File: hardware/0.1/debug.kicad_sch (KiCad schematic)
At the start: 9 parts

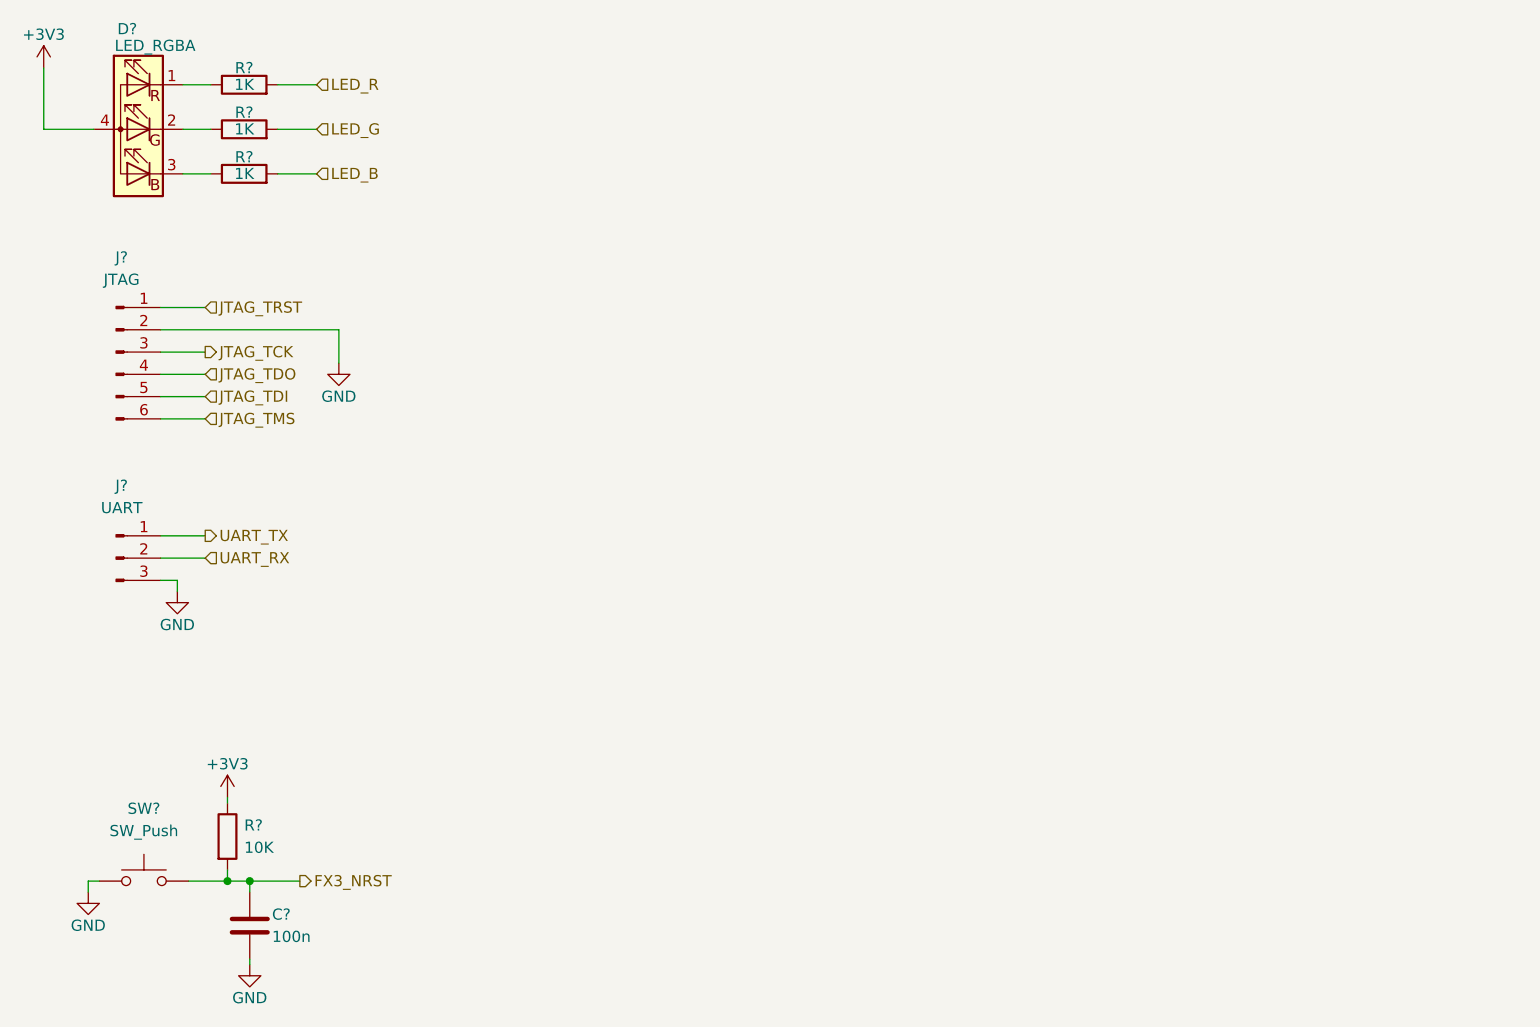
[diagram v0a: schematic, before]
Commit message: first pass schematic done
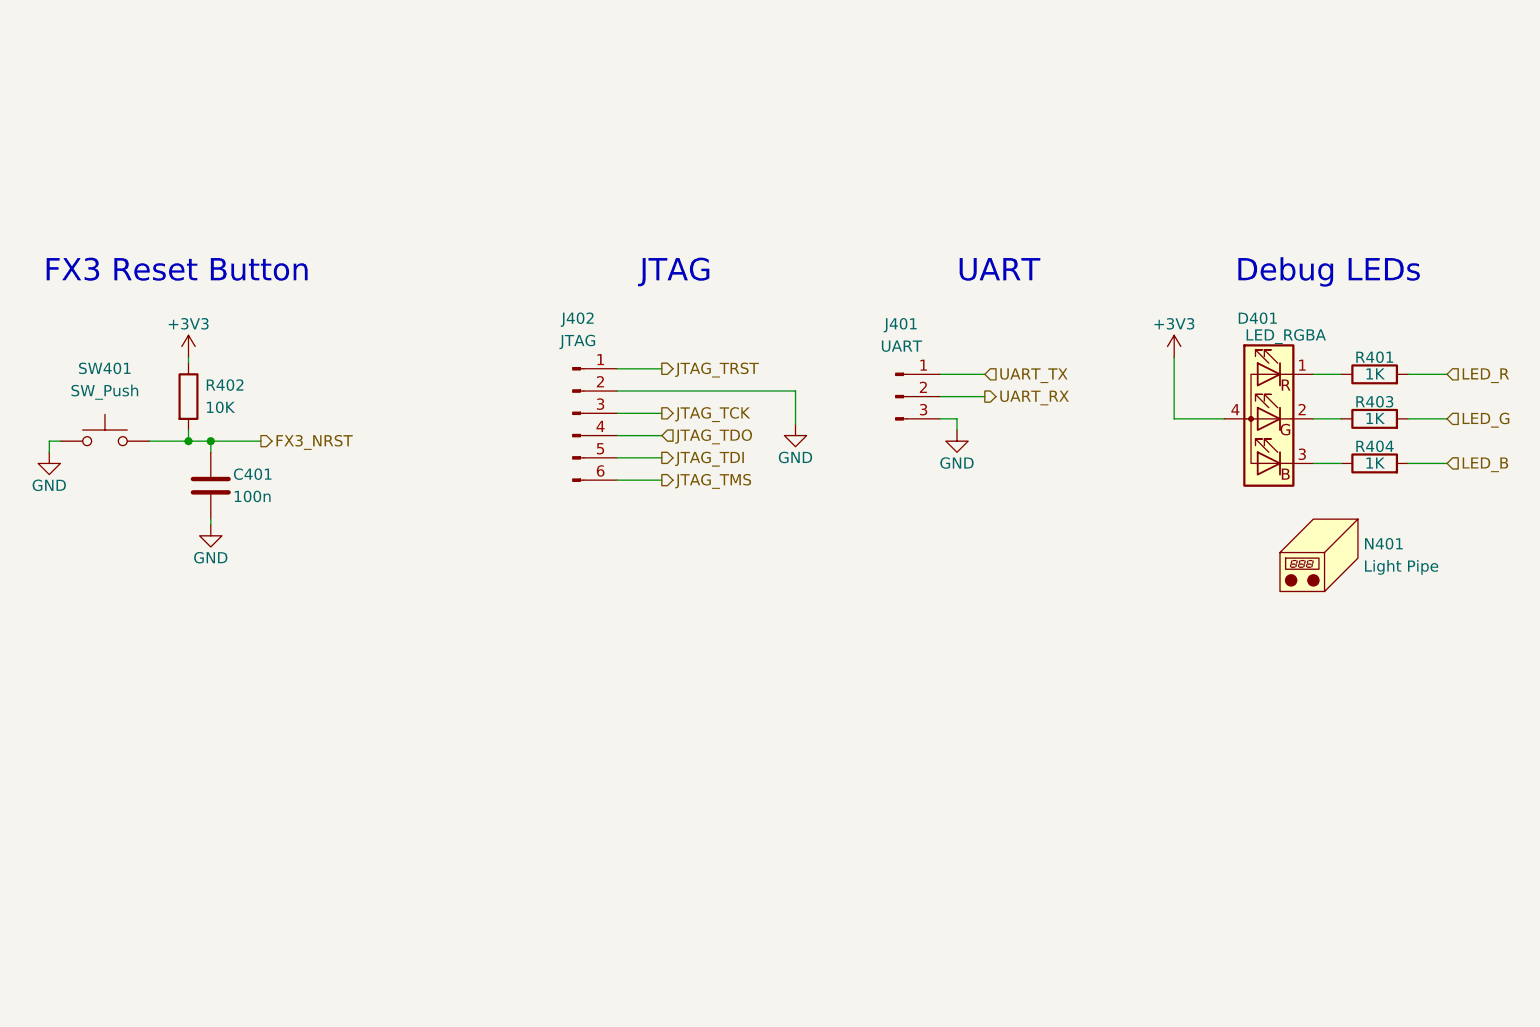
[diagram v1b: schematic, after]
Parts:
- added N401: Light Pipe, symbol Mechanical:Housing
- C401: renamed from C?; footprint (none) -> Capacitor_SMD:C_0402_1005Metric; LCSC (none) -> C307331; MPN (none) -> CL05B104KB54PNC; Manufacturer (none) -> Samsung Electro-Mechanics
- D401: renamed from D?; footprint (none) -> josh-led:LED_TRI_2020; LCSC (none) -> C108793; MPN (none) -> FM-B2020RGBA-HG; Manufacturer (none) -> Foshan NationStar Optoelectronics
- J401, J402: renamed from J?; now left out of the parts list
- R401, R403, R404: renamed from R?; footprint (none) -> Resistor_SMD:R_0402_1005Metric; LCSC (none) -> C144789; MPN (none) -> AC0402FR-071KL; Manufacturer (none) -> Yageo
- R402: renamed from R?; footprint (none) -> Resistor_SMD:R_0402_1005Metric; LCSC (none) -> C60490; MPN (none) -> RC0402FR-0710KL; Manufacturer (none) -> Yageo
- SW401: renamed from SW?; footprint (none) -> josh-buttons-switches:SW_PUSH_EVQPUL_EVQPUC; LCSC (none) -> C79174; MPN (none) -> EVQPUC02K; Manufacturer (none) -> Panasonic
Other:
- note added: "Debug LEDs"
- note added: "FX3 Reset Button"
- note added: "JTAG"
- note added: "UART"
- company: (none) -> Josh Johnson
- title: (none) -> Voyager Logic
- moved on the sheet: C401, D401, J401, J402, R401, R402, R403, R404, SW401

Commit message: finalise BOM
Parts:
- removed J401: UART, symbol Connector:Conn_01x03_Male
- removed N401: Light Pipe, symbol Mechanical:Housing
- added D402: LED_RGBA, josh-led:LED_TRI_2020, symbol josh-led:LED_RGBA
- added J401: JTAG, Connector:Tag-Connect_TC2030-IDC-NL_2x03_P1.27mm_Vertical, symbol Connector:Conn_01x06_Male
- added R405, R406, R407: 1K, Resistor_SMD:R_0402_1005Metric, symbol Device:R
- added R408: DNP, Resistor_SMD:R_0402_1005Metric, symbol Device:R
- added R409: 0R0, Resistor_SMD:R_0402_1005Metric, symbol Device:R
- J402: footprint (none) -> Connector:Tag-Connect_TC2030-IDC-NL_2x03_P1.27mm_Vertical
- SW401: value SW_Push -> KMR2; footprint josh-buttons-switches:SW_PUSH_EVQPUL_EVQPUC -> josh-buttons-switches:SW_Push_KMR2; LCSC C79174 -> (none); MPN EVQPUC02K -> (none); Manufacturer Panasonic -> (none)
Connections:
- net +3V3: now also D402.4 (A), R408.2
- net GND: now also J402.5 (Pin_5), J401.3 (Pin_3), R405.2, R406.2, R407.2; no longer J402.2 (Pin_2)
- net JTAG_TCK: now also J402.4 (Pin_4); no longer J402.3 (Pin_3)
- net JTAG_TDI: now also J402.3 (Pin_3); no longer J402.5 (Pin_5)
- net JTAG_TDO: now also J402.6 (Pin_6); no longer J402.4 (Pin_4)
- net JTAG_TMS: now also J402.2 (Pin_2); no longer J402.6 (Pin_6)
- net JTAG_TRST: now also R409.2; no longer J402.1 (Pin_1)
- net UART_RX: now also J401.2 (Pin_2)
- net UART_TX: now also J401.1 (Pin_1)
- new net: D402.1 (RK), R405.1
- new net: D402.2 (GK), R406.1
- new net: D402.3 (BK), R407.1
- new net: J402.1 (Pin_1), R408.1, R409.1
- no-connect marks 0 -> 3
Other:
- note added: "Digilent HS2/3 pinout has 3v3 on pin 1 We need to breakout JTAG_TRST So placing them on the same pin"
- note added: "Used for power indication"

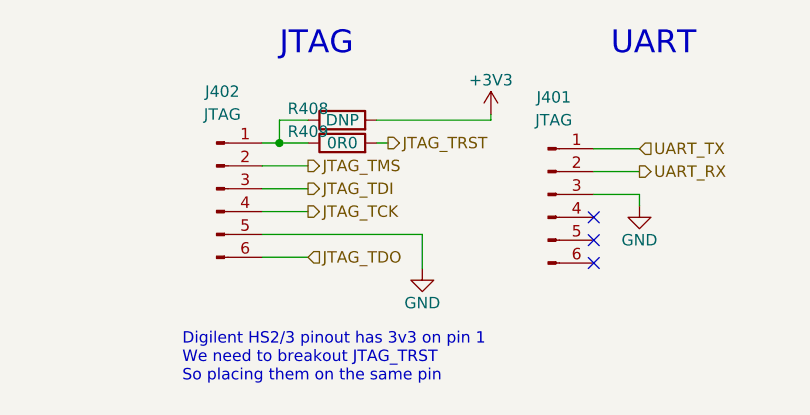
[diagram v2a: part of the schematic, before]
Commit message: all components fit inside outline
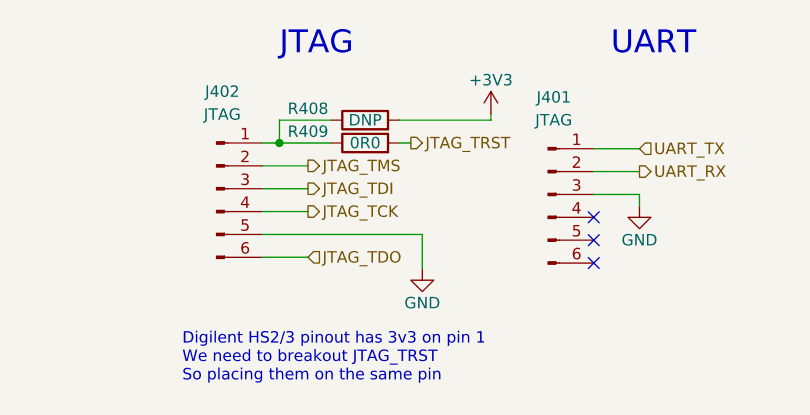
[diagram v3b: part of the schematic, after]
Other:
- moved on the sheet: R408, R409
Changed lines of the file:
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@@
+    (stroke (width 0) (type default) (color 0 0 0 0))
+  )
+  (wire (pts (xy 128.27 97.79) (xy 123.19 97.79))
+    (stroke (width 0) (type default) (color 0 0 0 0))
+  )
+  (wire (pts (xy 123.19 92.71) (xy 128.27 92.71))
+    (stroke (width 0) (type default) (color 0 0 0 0))
+  )
+  (wire (pts (xy 140.97 100.33) (xy 140.97 104.14))
+    (stroke (width 0) (type default) (color 0 0 0 0))
+  )
+  (wire (pts (xy 74.295 88.9) (xy 74.295 89.535))
+    (stroke (width 0) (type default) (color 0 0 0 0))
+  )
+  (wire (pts (xy 202.565 95.885) (xy 205.74 95.885))
+    (stroke (width 0) (type default) (color 0 0 0 0))
+  )
+  (wire (pts (xy 217.805 117.475) (xy 217.805 122.555))
+    (stroke (width 0) (type default) (color 0 0 0 0))
+  )
+  (wire (pts (xy 202.565 117.475) (xy 205.74 117.475))
+    (stroke (width 0) (type default) (color 0 0 0 0))
+  )
+  (wire (pts (xy 213.36 127.635) (xy 217.805 127.635))
+    (stroke (width 0) (type default) (color 0 0 0 0))
+  )
+  (wire (pts (xy 202.565 90.805) (xy 205.74 90.805))
+    (stroke (width 0) (type default) (color 0 0 0 0))
+  )
+  (wire (pts (xy 74.295 97.155) (xy 74.295 98.425))
+    (stroke (width 0) (type default) (color 0 0 0 0))
+  )
+  (wire (pts (xy 213.36 90.805) (xy 217.805 90.805))
+    (stroke (width 0) (type default) (color 0 0 0 0))
+  )
+  (wire (pts (xy 217.805 122.555) (xy 217.805 127.635))
+    (stroke (width 0) (type default) (color 0 0 0 0))
+  )
+  (wire (pts (xy 165.1 90.805) (xy 160.02 90.805))
+    (stroke (width 0) (type default) (color 0 0 0 0))
+  )
+  (wire (pts (xy 202.565 127.635) (xy 205.74 127.635))
+    (stroke (width 0) (type default) (color 0 0 0 0))
+  )
+  (wire (pts (xy 76.835 99.695) (xy 76.835 98.425))
+    (stroke (width 0) (type default) (color 0 0 0 0))
+  )
+  (wire (pts (xy 213.36 117.475) (xy 217.805 117.475))
+    (stroke (width 0) (type default) (color 0 0 0 0))
+  )
+  (wire (pts (xy 186.69 115.57) (xy 186.69 122.555))
+    (stroke (width 0) (type default) (color 0 0 0 0))
+  )
+  (wire (pts (xy 160.02 95.885) (xy 165.1 95.885))
+    (stroke (width 0) (type default) (color 0 0 0 0))
+  )
+  (wire (pts (xy 130.81 87.63) (xy 125.095 87.63))
+    (stroke (width 0) (type default) (color 0 0 0 0))
+  )
+  (wire (pts (xy 138.43 87.63) (xy 148.59 87.63))
+    (stroke (width 0) (type default) (color 0 0 0 0))
+  )
+  (wire (pts (xy 192.405 95.885) (xy 186.69 95.885))
+    (stroke (width 0) (type default) (color 0 0 0 0))
+  )
+  (wire (pts (xy 165.1 93.345) (xy 160.02 93.345))
+    (stroke (width 0) (type default) (color 0 0 0 0))
+  )
+  (wire (pts (xy 125.095 90.17) (xy 130.81 90.17))
+    (stroke (width 0) (type default) (color 0 0 0 0))
+  )
+  (wire (pts (xy 202.565 100.965) (xy 205.74 100.965))
+    (stroke (width 0) (type default) (color 0 0 0 0))
+  )
+  (wire (pts (xy 59.69 98.425) (xy 58.42 98.425))
+    (stroke (width 0) (type default) (color 0 0 0 0))
+  )
+  (wire (pts (xy 125.095 90.17) (xy 123.19 90.17))
+    (stroke (width 0) (type default) (color 0 0 0 0))
+  )
+  (wire (pts (xy 138.43 90.17) (xy 139.7 90.17))
+    (stroke (width 0) (type default) (color 0 0 0 0))
+  )
+  (wire (pts (xy 125.095 87.63) (xy 125.095 90.17))
+    (stroke (width 0) (type default) (color 0 0 0 0))
+  )
+  (wire (pts (xy 74.295 98.425) (xy 76.835 98.425))
+    (stroke (width 0) (type default) (color 0 0 0 0))
+  )
+  (wire (pts (xy 213.36 122.555) (xy 217.805 122.555))
+    (stroke (width 0) (type default) (color 0 0 0 0))
+  )
+  (wire (pts (xy 217.805 127.635) (xy 217.805 129.54))
     (stroke (width 0) (type default) (color 0 0 0 0))
   )
   (wire (pts (xy 148.59 86.995) (xy 148.59 87.63))
-    (stroke (width 0) (type default) (color 0 0 0 0))
-  )
-  (wire (pts (xy 128.27 97.79) (xy 123.19 97.79))
-    (stroke (width 0) (type default) (color 0 0 0 0))
-  )
-  (wire (pts (xy 123.19 92.71) (xy 128.27 92.71))
-    (stroke (width 0) (type default) (color 0 0 0 0))
-  )
-  (wire (pts (xy 140.97 100.33) (xy 140.97 104.14))
-    (stroke (width 0) (type default) (color 0 0 0 0))
-  )
-  (wire (pts (xy 74.295 88.9) (xy 74.295 89.535))
-    (stroke (width 0) (type default) (color 0 0 0 0))
-  )
-  (wire (pts (xy 202.565 95.885) (xy 205.74 95.885))
-    (stroke (width 0) (type default) (color 0 0 0 0))
-  )
-  (wire (pts (xy 217.805 117.475) (xy 217.805 122.555))
-    (stroke (width 0) (type default) (color 0 0 0 0))
-  )
-  (wire (pts (xy 202.565 117.475) (xy 205.74 117.475))
-    (stroke (width 0) (type default) (color 0 0 0 0))
-  )
-  (wire (pts (xy 213.36 127.635) (xy 217.805 127.635))
-    (stroke (width 0) (type default) (color 0 0 0 0))
-  )
-  (wire (pts (xy 202.565 90.805) (xy 205.74 90.805))
-    (stroke (width 0) (type default) (color 0 0 0 0))
-  )
-  (wire (pts (xy 74.295 97.155) (xy 74.295 98.425))
-    (stroke (width 0) (type default) (color 0 0 0 0))
-  )
-  (wire (pts (xy 213.36 90.805) (xy 217.805 90.805))
-    (stroke (width 0) (type default) (color 0 0 0 0))
-  )
-  (wire (pts (xy 217.805 122.555) (xy 217.805 127.635))
-    (stroke (width 0) (type default) (color 0 0 0 0))
-  )
-  (wire (pts (xy 165.1 90.805) (xy 160.02 90.805))
-    (stroke (width 0) (type default) (color 0 0 0 0))
-  )
-  (wire (pts (xy 202.565 127.635) (xy 205.74 127.635))
-    (stroke (width 0) (type default) (color 0 0 0 0))
-  )
-  (wire (pts (xy 76.835 99.695) (xy 76.835 98.425))
-    (stroke (width 0) (type default) (color 0 0 0 0))
-  )
-  (wire (pts (xy 213.36 117.475) (xy 217.805 117.475))
-    (stroke (width 0) (type default) (color 0 0 0 0))
-  )
-  (wire (pts (xy 186.69 115.57) (xy 186.69 122.555))
-    (stroke (width 0) (type default) (color 0 0 0 0))
-  )
-  (wire (pts (xy 160.02 95.885) (xy 165.1 95.885))
-    (stroke (width 0) (type default) (color 0 0 0 0))
-  )
-  (wire (pts (xy 128.27 87.63) (xy 125.095 87.63))
-    (stroke (width 0) (type default) (color 0 0 0 0))
-  )
-  (wire (pts (xy 192.405 95.885) (xy 186.69 95.885))
-    (stroke (width 0) (type default) (color 0 0 0 0))
-  )
-  (wire (pts (xy 165.1 93.345) (xy 160.02 93.345))
-    (stroke (width 0) (type default) (color 0 0 0 0))
-  )
-  (wire (pts (xy 125.095 90.17) (xy 128.27 90.17))
-    (stroke (width 0) (type default) (color 0 0 0 0))
-  )
-  (wire (pts (xy 202.565 100.965) (xy 205.74 100.965))
-    (stroke (width 0) (type default) (color 0 0 0 0))
-  )
-  (wire (pts (xy 59.69 98.425) (xy 58.42 98.425))
-    (stroke (width 0) (type default) (color 0 0 0 0))
-  )
-  (wire (pts (xy 125.095 90.17) (xy 123.19 90.17))
-    (stroke (width 0) (type default) (color 0 0 0 0))
-  )
-  (wire (pts (xy 135.89 90.17) (xy 137.16 90.17))
-    (stroke (width 0) (type default) (color 0 0 0 0))
-  )
-  (wire (pts (xy 125.095 87.63) (xy 125.095 90.17))
-    (stroke (width 0) (type default) (color 0 0 0 0))
-  )
-  (wire (pts (xy 74.295 98.425) (xy 76.835 98.425))
-    (stroke (width 0) (type default) (color 0 0 0 0))
-  )
-  (wire (pts (xy 213.36 122.555) (xy 217.805 122.555))
-    (stroke (width 0) (type default) (color 0 0 0 0))
-  )
-  (wire (pts (xy 135.89 87.63) (xy 148.59 87.63))
-    (stroke (width 0) (type default) (color 0 0 0 0))
-  )
-  (wire (pts (xy 217.805 127.635) (xy 217.805 129.54))
     (stroke (width 0) (type default) (color 0 0 0 0))
   )
@@
     (effects (font (size 1.27 1.27)) (justify left))
   )
-  (hierarchical_label "JTAG_TRST" (shape output) (at 137.16 90.17 0)
+  (hierarchical_label "JTAG_TRST" (shape output) (at 139.7 90.17 0)
     (effects (font (size 1.27 1.27)) (justify left))
   )
@@
     (pin "4")
   )
-  (symbol (lib_id "Device:R") (at 132.08 87.63 90) (unit 1)
+  (symbol (lib_id "Device:R") (at 134.62 87.63 90) (unit 1)
     (in_bom yes) (on_board yes)
     (property "Reference" "R408" (id 0) (at 128.27 86.36 90))
-    (property "Value" "DNP" (id 1) (at 132.08 87.63 90))
-    (property "Footprint" "Resistor_SMD:R_0402_1005Metric" (id 2) (at 132.08 89.408 90)
-      (effects (font (size 1.27 1.27)) hide)
-    )
-    (property "Datasheet" "~" (id 3) (at 132.08 87.63 0)
+    (property "Value" "DNP" (id 1) (at 134.62 87.63 90))
+    (property "Footprint" "Resistor_SMD:R_0402_1005Metric" (id 2) (at 134.62 89.408 90)
+      (effects (font (size 1.27 1.27)) hide)
+    )
+    (property "Datasheet" "~" (id 3) (at 134.62 87.63 0)
       (effects (font (size 1.27 1.27)) hide)
     )
@@
     (pin "1")
   )
-  (symbol (lib_id "Device:R") (at 132.08 90.17 90) (unit 1)
+  (symbol (lib_id "Device:R") (at 134.62 90.17 90) (unit 1)
     (in_bom yes) (on_board yes)
     (property "Reference" "R409" (id 0) (at 128.27 88.9 90))
-    (property "Value" "0R0" (id 1) (at 132.08 90.17 90))
-    (property "Footprint" "Resistor_SMD:R_0402_1005Metric" (id 2) (at 132.08 91.948 90)
-      (effects (font (size 1.27 1.27)) hide)
-    )
-    (property "Datasheet" "~" (id 3) (at 132.08 90.17 0)
-      (effects (font (size 1.27 1.27)) hide)
-    )
+    (property "Value" "0R0" (id 1) (at 134.62 90.17 90))
+    (property "Footprint" "Resistor_SMD:R_0402_1005Metric" (id 2) (at 134.62 91.948 90)
+      (effects (font (size 1.27 1.27)) hide)
+    )
+    (property "Datasheet" "~" (id 3) (at 134.62 90.17 0)
+      (effects (font (size 1.27 1.27)) hide)
+    )

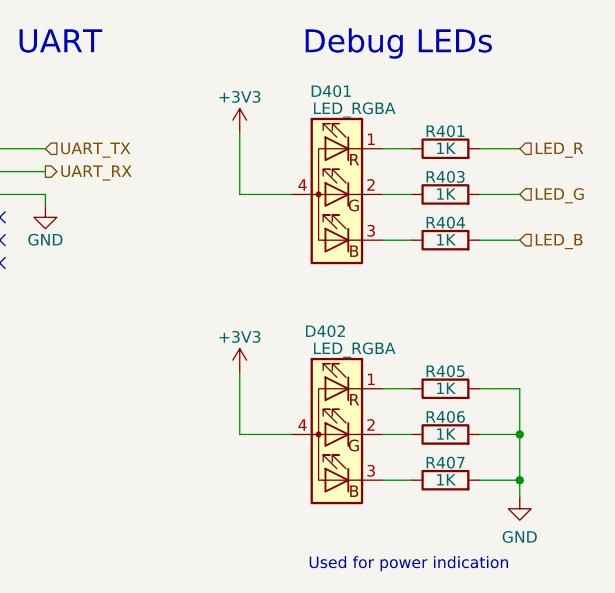
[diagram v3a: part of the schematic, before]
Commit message: break out bga
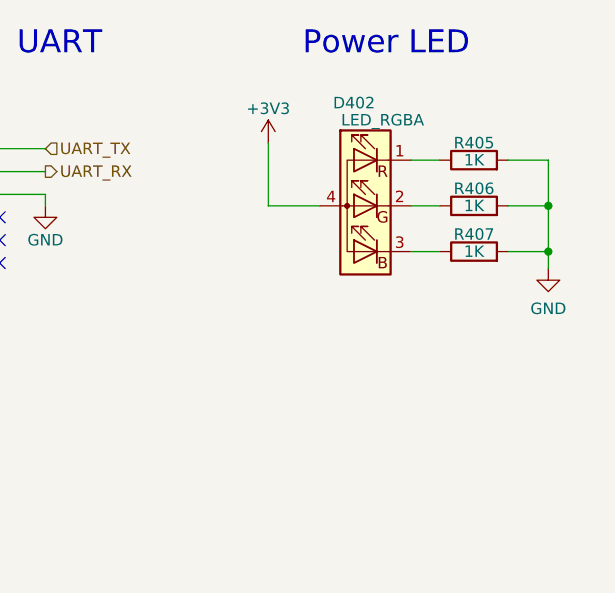
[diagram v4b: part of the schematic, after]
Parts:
- removed D401: LED_RGBA, josh-led:LED_TRI_2020, symbol josh-led:LED_RGBA
- removed R401, R403, R404: 1K, Resistor_SMD:R_0402_1005Metric, symbol Device:R
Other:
- note added: "Power LED"
- note removed: "Debug LEDs"
- note removed: "Used for power indication"
- moved on the sheet: D402, R405, R406, R407
